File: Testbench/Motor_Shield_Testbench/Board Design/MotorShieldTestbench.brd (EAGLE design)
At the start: 160 x 100 mm, 92 parts, among them IC1 74LS157D, IC3 74AC74D, IC4 74AC74D, J2 MICRO-SD_CARD_SOCKET, U1 LPC1768FBD100, U2 SN74HC04DR, U3 ATTINY85-20SU, U4 ATTINY85-20SU, U5 DUAL-OPTOISOLATOR_SOIC8, U6 DUAL-OPTOISOLATOR_SOIC8, U7 DUAL-OPTOISOLATOR_SOIC8, U8 DUAL-OPTOISOLATOR_SOIC8, X1 C-GRID-05-15-91, X2 C-GRID-05-15-91, X4 2510-, X5 2510-, X6 MINI-USB_4P-32005-101, X7 2510-, X8 2510-, Y1 32.768kHz, Y2 12MHz

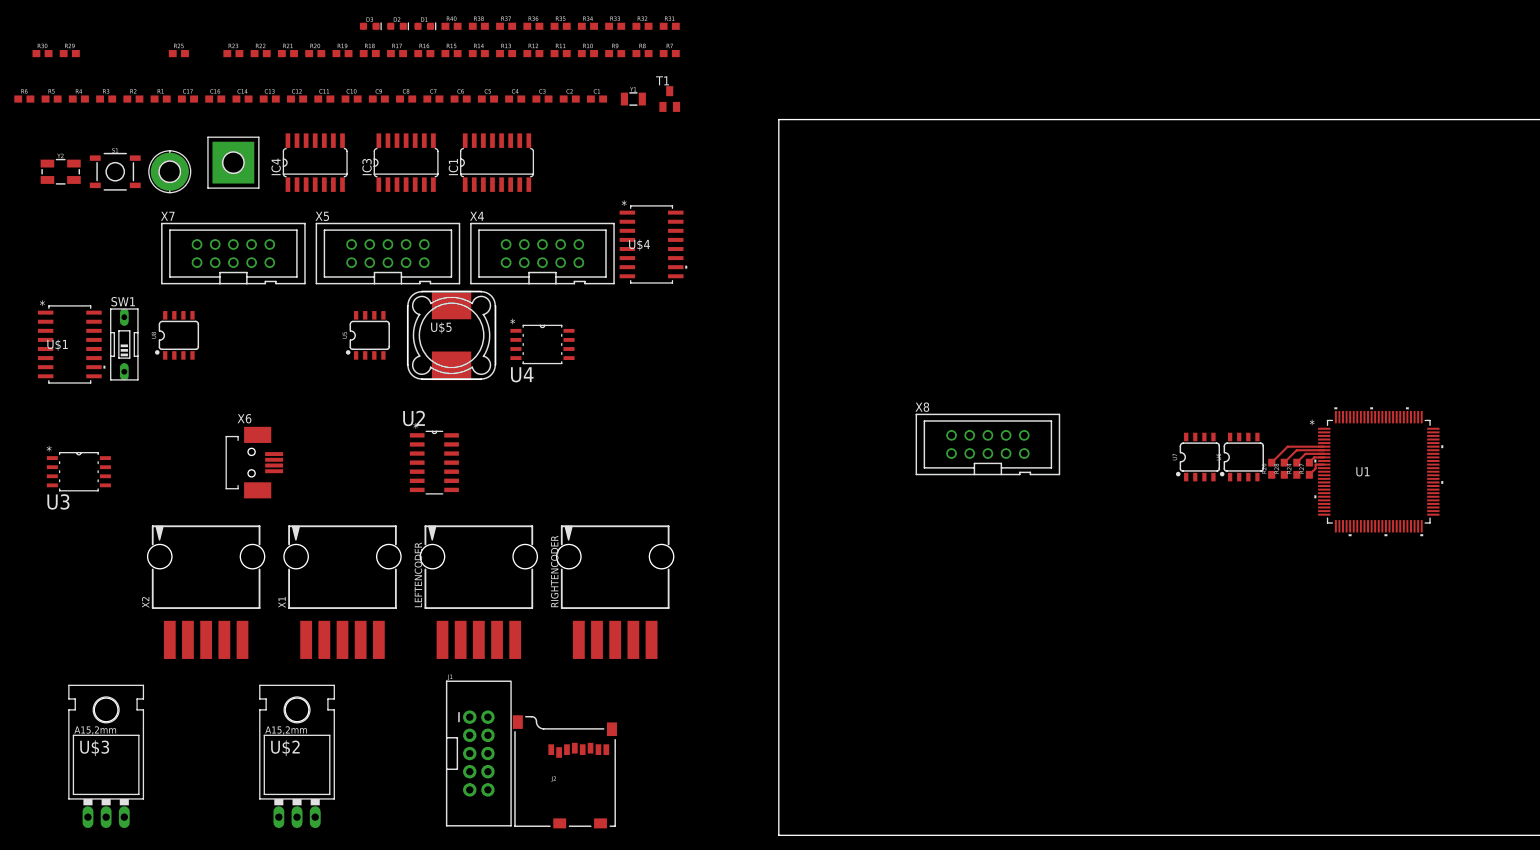
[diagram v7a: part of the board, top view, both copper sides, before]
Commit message: standoff libr
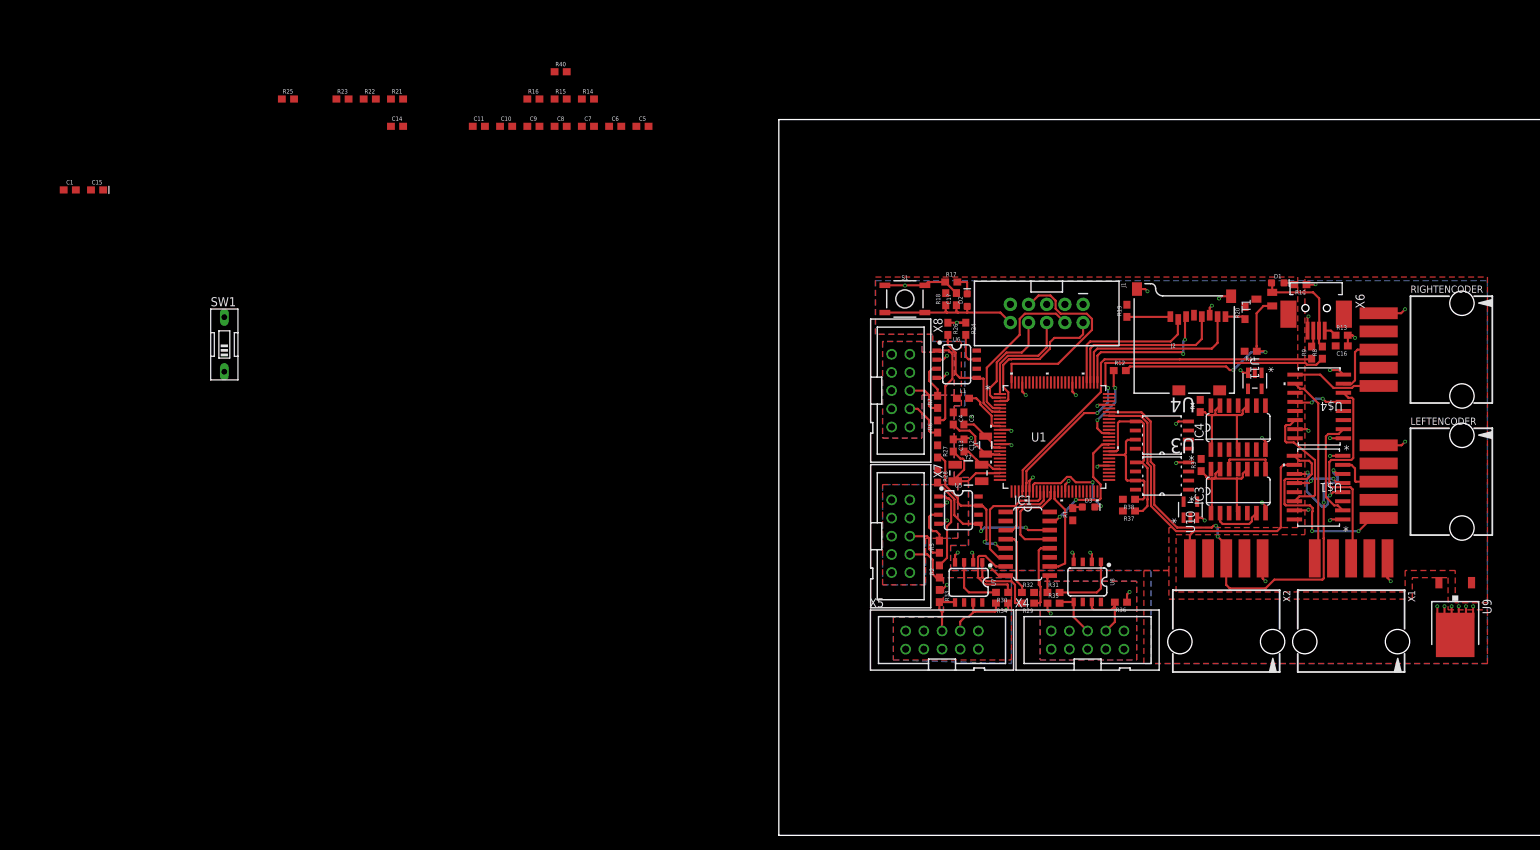
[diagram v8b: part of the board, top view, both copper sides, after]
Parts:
- removed C2: 1.0uF, SparkFun-Capacitors:0603
- removed H1: MOUNT-PAD-ROUND2.8, holes:2,8-PAD
- removed H2: MOUNT-PAD-SQUARE2.8, holes:2,8-PAD-SQUARE
- removed U$2, U$3: V_REG_LD1117VXX, SparkFun-IC-Power:78XXL
- removed U$5: 10uH, inductor-coilcraft:MSS1260
- removed U2: SN74HC04DR, Texas Instruments_By_element14_Batch_1:SOIC127P600X175-14N
- added C15: 10uF, SparkFun-Capacitors:0603-POLAR
- added L1: 10uH, SparkFun-Coils:0603
- added U10, U11: SN74LVC1G04DBVR, zilog:DBV5
- added U9: +12v, SparkFun-IC-Power:TO-252
- C1: value 10nF -> 0.1uF
- moved U$1 175.6 mm to (75.4, 48.6), turned to 180 degrees
- moved R4 162.4 mm to (58.9, 60.0), turned to 90 degrees
- moved R3 161.3 mm to (59.0, 51.7), turned to 90 degrees
- moved C16 161.1 mm to (78.7, 68.4), turned to 180 degrees
- moved R29 154.3 mm to (34.8, 32.4), turned to 180 degrees
- moved R30 153.8 mm to (31.2, 33.9), turned to 180 degrees
- moved U3 151.3 mm to (53.5, 50.2), turned to 180 degrees
- moved X6 150.3 mm to (75.1, 73.7), turned to 270 degrees
- moved X2 142.9 mm to (62.5, 27.9), turned to 180 degrees
- moved X1 141.3 mm to (80.0, 27.9), turned to 180 degrees
- moved R1 140.0 mm to (41.1, 44.9), turned to 90 degrees
- moved R5 138.9 mm to (22.4, 40.3), turned to 90 degrees
- moved LEFTENCODER 137.0 mm to (94.6, 49.4), turned to 270 degrees
- moved R6 135.6 mm to (22.2, 57.1), turned to 90 degrees
- moved R20 134.9 mm to (65.1, 73.0), turned to 90 degrees
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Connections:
- removed net LDIRIN1: X8.8
- removed net N$33: H2.B2,8, U$2.OUT
- removed net RDIRIN1: X7.8
- removed net VDD: IC1.16, IC3.14, IC4.14, R11.2, R18.2, R3.2, R4.2, T1.C, U$2.GND, U$3.GND, U2.14
- net +3V3: now also C1.1, C15.+, IC1.16, IC3.14, IC4.14, L1.1, R11.2, R18.2, R3.2, R4.2, T1.C, U1.13, U10.5, U11.5, U9.2; no longer U$5.P$1
- net +3V3A: now also L1.2; no longer C1.1, C2.1, U$5.P$2
- net +5V: now also U9.1; no longer U$3.OUT
- net GND: now also C15.-, U$1.1, U$1.15, U$4.1, U$4.15, U10.3, U11.3, U9.3; no longer C2.2, H1.B2,8, R33.1, R34.1, R35.1, R36.1, U$2.IN, U$3.IN, U2.7
- net LDIR: now also R29.1; no longer R30.1
- net LDIR1: now also R34.2, U7.7; no longer R33.2, U7.5
- net LDIRIN: now also R6.1, X8.8; no longer IC1.14, R5.1
- net LDIRIN3: now also IC1.14
- net LDIRO: now also U1.37; no longer U1.35
- net LEIN1: no longer U3.2
- net LEIN2: no longer U3.3
- net LGND: now also R33.1, R34.1
- net LSPEED: now also U1.9; no longer C9.1, IC1.5, R15.2
- net LSPEEDH: now also R30.1; no longer R29.1
- net LSPEEDH1: now also R33.2, U7.5; no longer R34.2, U7.7
- net LSPEEDIN3: now also IC1.5; no longer U1.9
- net LSPEEDO: now also U1.34; no longer U1.37
- net LWAVE: now also U10.2; no longer U2.1
- net LWAVE*: now also U10.4; no longer U2.2
- net RDIR: now also R31.1; no longer R32.1
- net RDIR1: now also R36.2, U8.7; no longer R35.2, U8.5
- net RDIRIN: now also X7.8; no longer IC1.11
- net RDIRIN3: now also IC1.11
- net RDIRO: now also U1.38; no longer U1.36
- net REIN1: no longer U4.2
- net REIN2: no longer U4.3
- net RGND: now also R35.1, R36.1
- net RSPEED: now also C9.1, R15.2, U1.8; no longer IC1.2
- net RSPEEDH: now also R32.1; no longer R31.1
- net RSPEEDH1: now also R35.2, U8.5; no longer R36.2, U8.7
- net RSPEEDIN: now also R5.1; no longer R6.1
- net RSPEEDIN3: now also IC1.2; no longer U1.8
- net RSPEEDO: now also U1.35; no longer U1.38
- net RST: no longer U3.1, U4.1
- net RWAVE: now also U11.2; no longer U2.3
- net RWAVE*: now also U11.4; no longer U2.4
- net STOP: no longer U$1.1, U$1.15, U$4.1, U$4.15
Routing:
- net GND: track 2.96 -> 98.5 mm, vias 0 -> 45
- net LEIN1: track 0.00 -> 70.0 mm, vias 0 -> 4
- net DM: track 0.00 -> 54.7 mm, vias 0 -> 2
- net DP: track 0.00 -> 52.2 mm
- net LEIN2: track 0.00 -> 51.9 mm
- net N$22: track 0.00 -> 30.2 mm, vias 0 -> 2
- net REIN1: track 0.00 -> 30.1 mm
- net LE2: track 0.00 -> 29.6 mm, vias 0 -> 2
- net RTCK: track 0.00 -> 28.7 mm
- net REIN2: track 0.00 -> 26.3 mm
- net SD_DO: track 0.00 -> 25.7 mm
- net SD_SCK: track 0.00 -> 24.0 mm
- net SDA: track 0.00 -> 23.8 mm
- net TCK: track 0.00 -> 22.8 mm
- net TMS: track 0.00 -> 21.5 mm
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- added copper zone on layer 1, net +3V3
- added copper zone on layer 1, net +5V
- added copper zone on layer 16, net GND
- added copper zone on layer 1, net L+12V
- added copper zone on layer 16, net LGND
- added copper zone on layer 1, net R+12V
- added copper zone on layer 16, net RGND
